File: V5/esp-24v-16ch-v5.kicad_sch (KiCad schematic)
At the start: 4 parts, among them J1 DB141V-2.54-8P, J2 DB141V-2.54-8P, J3 DB141V-2.54-8P, J4 DB141V-2.54-8P

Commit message: Created V5
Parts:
- added FID1, FID2, FID3: Fiducial, Fiducial:Fiducial_1mm_Mask2mm, symbol Mechanical:Fiducial
- renumbered J1 to J5, J2 to J6, J3 to J7, J4 to J8
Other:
- sheet I2C Devices: file esp-24v-16ch-v4-i2c.kicad_sch -> esp-24v-16ch-v5-i2c.kicad_sch
- sheet I2C Devices ports: added I2CSCL, I2CSDA, MCPININTA, MCPININTB; removed I2C_SCL, I2C_SDA, MCP1-INTA, MCP1-INTB
- sheet Input 1: file esp-24v-16ch-v4-inputs.kicad_sch -> esp-24v-16ch-v5-inputs1-8.kicad_sch
- sheet Input 1 ports: added MUXIN; removed MUX_IN
- sheet Input 10: file esp-24v-16ch-v4-inputs.kicad_sch -> esp-24v-16ch-v5-inputs9-16.kicad_sch
- sheet Input 10 ports: added MUXIN; removed MUX_IN
- sheet Input 11: file esp-24v-16ch-v4-inputs.kicad_sch -> esp-24v-16ch-v5-inputs9-16.kicad_sch
- sheet Input 11 ports: added MUXIN; removed MUX_IN
- sheet Input 12: file esp-24v-16ch-v4-inputs.kicad_sch -> esp-24v-16ch-v5-inputs9-16.kicad_sch
- sheet Input 12 ports: added MUXIN; removed MUX_IN
- sheet Input 13: file esp-24v-16ch-v4-inputs.kicad_sch -> esp-24v-16ch-v5-inputs9-16.kicad_sch
- sheet Input 13 ports: added MUXIN; removed MUX_IN
- sheet Input 14: file esp-24v-16ch-v4-inputs.kicad_sch -> esp-24v-16ch-v5-inputs9-16.kicad_sch
- sheet Input 14 ports: added MUXIN; removed MUX_IN
- sheet Input 15: file esp-24v-16ch-v4-inputs.kicad_sch -> esp-24v-16ch-v5-inputs9-16.kicad_sch
- sheet Input 15 ports: added MUXIN; removed MUX_IN
- sheet Input 16: file esp-24v-16ch-v4-inputs.kicad_sch -> esp-24v-16ch-v5-inputs9-16.kicad_sch
- sheet Input 16 ports: added MUXIN; removed MUX_IN
- sheet Input 2: file esp-24v-16ch-v4-inputs.kicad_sch -> esp-24v-16ch-v5-inputs1-8.kicad_sch
- sheet Input 2 ports: added MUXIN; removed MUX_IN
- sheet Input 3: file esp-24v-16ch-v4-inputs.kicad_sch -> esp-24v-16ch-v5-inputs1-8.kicad_sch
- sheet Input 3 ports: added MUXIN; removed MUX_IN
- sheet Input 4: file esp-24v-16ch-v4-inputs.kicad_sch -> esp-24v-16ch-v5-inputs1-8.kicad_sch
- sheet Input 4 ports: added MUXIN; removed MUX_IN
- sheet Input 5: file esp-24v-16ch-v4-inputs.kicad_sch -> esp-24v-16ch-v5-inputs1-8.kicad_sch
- sheet Input 5 ports: added MUXIN; removed MUX_IN
- sheet Input 6: file esp-24v-16ch-v4-inputs.kicad_sch -> esp-24v-16ch-v5-inputs1-8.kicad_sch
- sheet Input 6 ports: added MUXIN; removed MUX_IN
- sheet Input 7: file esp-24v-16ch-v4-inputs.kicad_sch -> esp-24v-16ch-v5-inputs1-8.kicad_sch
- sheet Input 7 ports: added MUXIN; removed MUX_IN
- sheet Input 8: file esp-24v-16ch-v4-inputs.kicad_sch -> esp-24v-16ch-v5-inputs1-8.kicad_sch
- sheet Input 8 ports: added MUXIN; removed MUX_IN
- sheet Input 9: file esp-24v-16ch-v4-inputs.kicad_sch -> esp-24v-16ch-v5-inputs9-16.kicad_sch
- sheet Input 9 ports: added MUXIN; removed MUX_IN
- sheet LAN: file esp-24v-16ch-v4-lan.kicad_sch -> esp-24v-16ch-v5-lan.kicad_sch
- sheet LAN ports: added EMACCLK, EMACMDC, EMACMDIO, EMACRX, EMACRXD0, EMACRXD1, EMACTXD0, EMACTXD1, EMACTXEN; removed EMAC_CLK, EMAC_MDC, EMAC_MDIO, EMAC_RX, EMAC_RXD0, EMAC_RXD1, EMAC_TXD0, EMAC_TXD1, EMAC_TXEN
- sheet MCU: file esp-24v-16ch-v4-mcu.kicad_sch -> esp-24v-16ch-v5-mcu.kicad_sch
- sheet MCU ports: added EMACCLK, EMACMDC, EMACMDIO, EMACRX, EMACRXD0, EMACRXD1, EMACTXD0, EMACTXD1, EMACTXEN, I2CSCL, I2CSDA, MCPININTA, MCPININTB, PHYPWR, USBD+, USBD-; removed EMAC_CLK, EMAC_MDC, EMAC_MDIO, EMAC_RX, EMAC_RXD0, EMAC_RXD1, EMAC_TXD0, EMAC_TXD1, EMAC_TXEN, I2C_SCL, I2C_SDA, MCP1-INTA, MCP1-INTB, PHY_PWR, USB_D+, USB_D-
- sheet Output 1: file esp-24v-16ch-outputs.kicad_sch -> esp-24v-16ch-v5-outputs1-8.kicad_sch
- sheet Output 1 ports: added MUXOUT; removed MUX_OUT
- sheet Output 10: file esp-24v-16ch-outputs.kicad_sch -> esp-24v-16ch-v5-outputs9-16.kicad_sch
- sheet Output 10 ports: added MUXOUT; removed MUX_OUT
- sheet Output 11: file esp-24v-16ch-outputs.kicad_sch -> esp-24v-16ch-v5-outputs9-16.kicad_sch
- sheet Output 11 ports: added MUXOUT; removed MUX_OUT
- sheet Output 12: file esp-24v-16ch-outputs.kicad_sch -> esp-24v-16ch-v5-outputs9-16.kicad_sch
- sheet Output 12 ports: added MUXOUT; removed MUX_OUT
- sheet Output 13: file esp-24v-16ch-outputs.kicad_sch -> esp-24v-16ch-v5-outputs9-16.kicad_sch
- sheet Output 13 ports: added MUXOUT; removed MUX_OUT
- sheet Output 14: file esp-24v-16ch-outputs.kicad_sch -> esp-24v-16ch-v5-outputs9-16.kicad_sch
- sheet Output 14 ports: added MUXOUT; removed MUX_OUT
- sheet Output 15: file esp-24v-16ch-outputs.kicad_sch -> esp-24v-16ch-v5-outputs9-16.kicad_sch
- sheet Output 15 ports: added MUXOUT; removed MUX_OUT
- sheet Output 16: file esp-24v-16ch-outputs.kicad_sch -> esp-24v-16ch-v5-outputs9-16.kicad_sch
- sheet Output 16 ports: added MUXOUT; removed MUX_OUT
- sheet Output 2: file esp-24v-16ch-outputs.kicad_sch -> esp-24v-16ch-v5-outputs1-8.kicad_sch
- sheet Output 2 ports: added MUXOUT; removed MUX_OUT
- sheet Output 3: file esp-24v-16ch-outputs.kicad_sch -> esp-24v-16ch-v5-outputs1-8.kicad_sch
- sheet Output 3 ports: added MUXOUT; removed MUX_OUT
- sheet Output 4: file esp-24v-16ch-outputs.kicad_sch -> esp-24v-16ch-v5-outputs1-8.kicad_sch
- sheet Output 4 ports: added MUXOUT; removed MUX_OUT
- sheet Output 5: file esp-24v-16ch-outputs.kicad_sch -> esp-24v-16ch-v5-outputs1-8.kicad_sch
- sheet Output 5 ports: added MUXOUT; removed MUX_OUT
- sheet Output 6: file esp-24v-16ch-outputs.kicad_sch -> esp-24v-16ch-v5-outputs1-8.kicad_sch
- sheet Output 6 ports: added MUXOUT; removed MUX_OUT
- sheet Output 7: file esp-24v-16ch-outputs.kicad_sch -> esp-24v-16ch-v5-outputs1-8.kicad_sch
- sheet Output 7 ports: added MUXOUT; removed MUX_OUT
- sheet Output 8: file esp-24v-16ch-outputs.kicad_sch -> esp-24v-16ch-v5-outputs1-8.kicad_sch
- sheet Output 8 ports: added MUXOUT; removed MUX_OUT
- sheet Output 9: file esp-24v-16ch-outputs.kicad_sch -> esp-24v-16ch-v5-outputs9-16.kicad_sch
- sheet Output 9 ports: added MUXOUT; removed MUX_OUT
- sheet Power: file esp-24v-16ch-v4-power.kicad_sch -> esp-24v-16ch-v5-power.kicad_sch
- sheet Power ports: added PHYPWR, USBD+, USBD-; removed PHY_PWR, USB_D+, USB_D-
- title: ESP 24V 16xIn/16xOut/4xNTC Module -> ESP 24V 16xIn/16xOut/1-Wire Module

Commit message: Updates and corrections to SCH and PCB
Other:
- sheet I2C Devices ports: added 1WIREGPIO; removed none
- sheet MCU ports: added 1WIREGPIO; removed none
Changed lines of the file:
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@@
 	(wire
 		(pts
-			(xy 219.71 59.69) (xy 219.71 71.12)
+			(xy 215.9 59.69) (xy 215.9 71.12)
 		)
 		(stroke
@@
 	(wire
 		(pts
-			(xy 214.63 59.69) (xy 214.63 71.12)
+			(xy 210.82 59.69) (xy 210.82 71.12)
 		)
 		(stroke
@@
 	(wire
 		(pts
-			(xy 212.09 59.69) (xy 212.09 71.12)
+			(xy 208.28 59.69) (xy 208.28 71.12)
 		)
 		(stroke
@@
 	(wire
 		(pts
+			(xy 222.25 59.69) (xy 222.25 71.12)
+		)
+		(stroke
+			(width 0)
+			(type default)
+		)
+	)
+	(wire
+		(pts
 			(xy 39.37 193.04) (xy 43.18 193.04)
 		)
@@
 	(wire
 		(pts
-			(xy 222.25 59.69) (xy 222.25 71.12)
+			(xy 218.44 59.69) (xy 218.44 71.12)
 		)
 		(stroke
@@
 		)
 		(pin "I2CSDA" bidirectional
-			(at 219.71 71.12 90)
+			(at 215.9 71.12 90)
 			(effects
 				(font
@@
 		)
 		(pin "I2CSCL" input
-			(at 222.25 71.12 90)
+			(at 218.44 71.12 90)
 			(effects
 				(font
@@
 		)
 		(pin "MCPININTB" output
-			(at 214.63 71.12 90)
+			(at 210.82 71.12 90)
 			(effects
 				(font
@@
 		)
 		(pin "MCPININTA" output
-			(at 212.09 71.12 90)
+			(at 208.28 71.12 90)
+			(effects
+				(font
+					(size 1.27 1.27)
+				)
+				(justify right)
+			)
+		)
+		(pin "1WIREGPIO" bidirectional
+			(at 222.25 71.12 90)
 			(effects
 				(font
@@
 		)
 		(pin "I2CSDA" bidirectional
-			(at 219.71 59.69 270)
+			(at 215.9 59.69 270)
 			(effects
 				(font
@@
 		)
 		(pin "I2CSCL" output
-			(at 222.25 59.69 270)
+			(at 218.44 59.69 270)
 			(effects
 				(font
@@
 		)
 		(pin "MCPININTA" input
-			(at 212.09 59.69 270)
+			(at 208.28 59.69 270)
 			(effects
 				(font
@@
 		)
 		(pin "MCPININTB" input
-			(at 214.63 59.69 270)
+			(at 210.82 59.69 270)
 			(effects
 				(font
@@
 			(effects
 				(font
+					(size 1.27 1.27)
+				)
+				(justify left)
+			)
+		)
+		(pin "1WIREGPIO" bidirectional
+			(at 222.25 59.69 270)
+			(effects
+				(font

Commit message: V5.2.0
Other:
- sheet MCU ports: added ESPEN; removed none
- sheet Power ports: added ESPEN; removed none
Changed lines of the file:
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@@
 	(wire
 		(pts
+			(xy 146.05 49.53) (xy 165.1 49.53)
+		)
+		(stroke
+			(width 0)
+			(type default)
+		)
+	)
+	(wire
+		(pts
 			(xy 276.86 166.37) (xy 265.43 166.37)
 		)
@@
 			)
 		)
-		(pin "USBD+" input
+		(pin "USBD+" bidirectional
 			(at 146.05 41.91 0)
 			(effects
@@
 			)
 		)
-		(pin "USBD-" input
+		(pin "USBD-" bidirectional
 			(at 146.05 44.45 0)
 			(effects
@@
 			)
 		)
+		(pin "ESPEN" output
+			(at 146.05 49.53 0)
+			(effects
+				(font
+					(size 1.27 1.27)
+				)
+				(justify right)
+			)
+		)
 		(instances
 			(project "esp-24v-16ch-v5"
@@
 			)
 		)
-		(pin "USBD+" input
+		(pin "USBD+" bidirectional
 			(at 165.1 41.91 180)
 			(effects
@@
 			)
 		)
-		(pin "USBD-" input
+		(pin "USBD-" bidirectional
 			(at 165.1 44.45 180)
 			(effects
@@
 			(effects
 				(font
+					(size 1.27 1.27)
+				)
+				(justify left)
+			)
+		)
+		(pin "ESPEN" input
+			(at 165.1 49.53 180)
+			(effects
+				(font

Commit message: Back to V5.1.0
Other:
- sheet MCU ports: added none; removed ESPEN
- sheet Power ports: added none; removed ESPEN
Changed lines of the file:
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@@
 	(wire
 		(pts
-			(xy 146.05 49.53) (xy 165.1 49.53)
-		)
-		(stroke
-			(width 0)
-			(type default)
-		)
-	)
-	(wire
-		(pts
 			(xy 276.86 166.37) (xy 265.43 166.37)
 		)
@@
 			)
 		)
-		(pin "ESPEN" output
-			(at 146.05 49.53 0)
-			(effects
-				(font
-					(size 1.27 1.27)
-				)
-				(justify right)
-			)
-		)
 		(instances
 			(project "esp-24v-16ch-v5"
@@
 			(effects
 				(font
-					(size 1.27 1.27)
-				)
-				(justify left)
-			)
-		)
-		(pin "ESPEN" input
-			(at 165.1 49.53 180)
-			(effects
-				(font

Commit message: Many changes!
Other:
- note added: "RESISTORS: 62,5mW WHERE NOT SPECIFIED"
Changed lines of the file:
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@@
 		(rev "V5.1")
+	)
+	(text "RESISTORS: 62,5mW WHERE NOT SPECIFIED"
+		(exclude_from_sim no)
+		(at 303.53 259.08 0)
+		(effects
+			(font
+				(size 1.905 1.905)
+			)
+			(justify left)
+		)
 	)
 	(wire

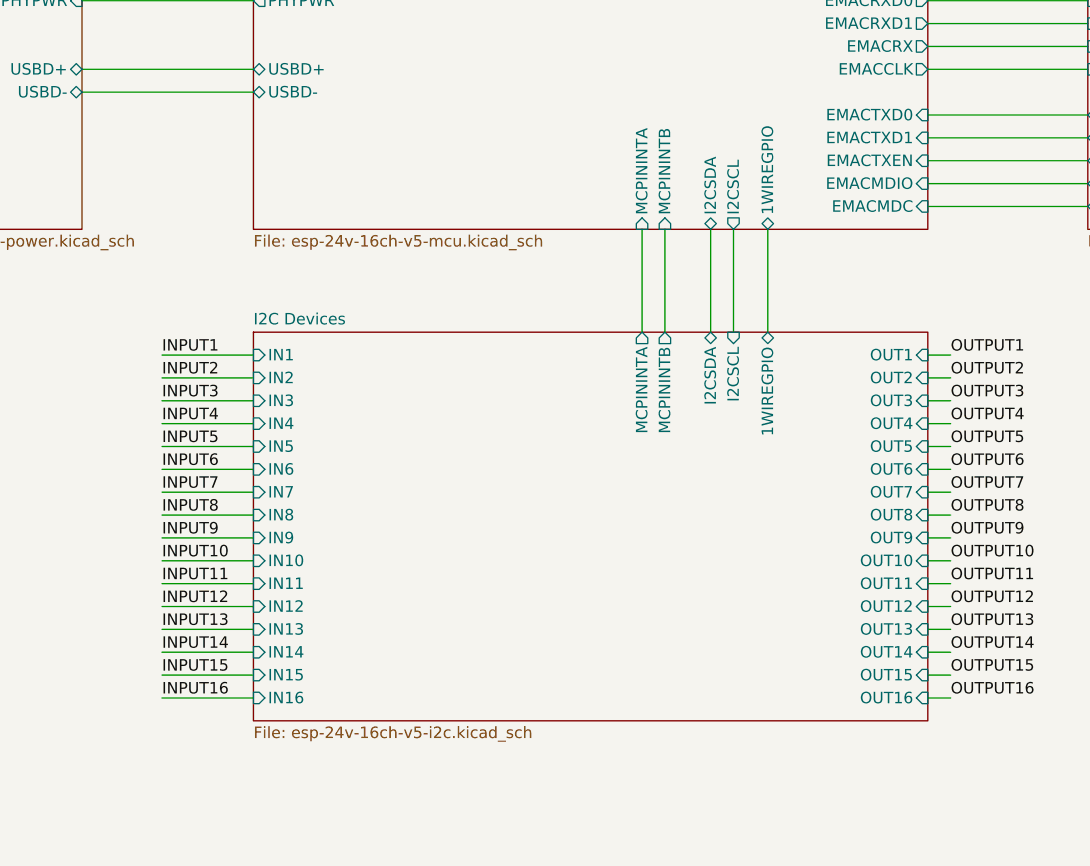
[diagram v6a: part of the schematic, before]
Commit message: MCP23017 GPA7 and GPB7 disabled.
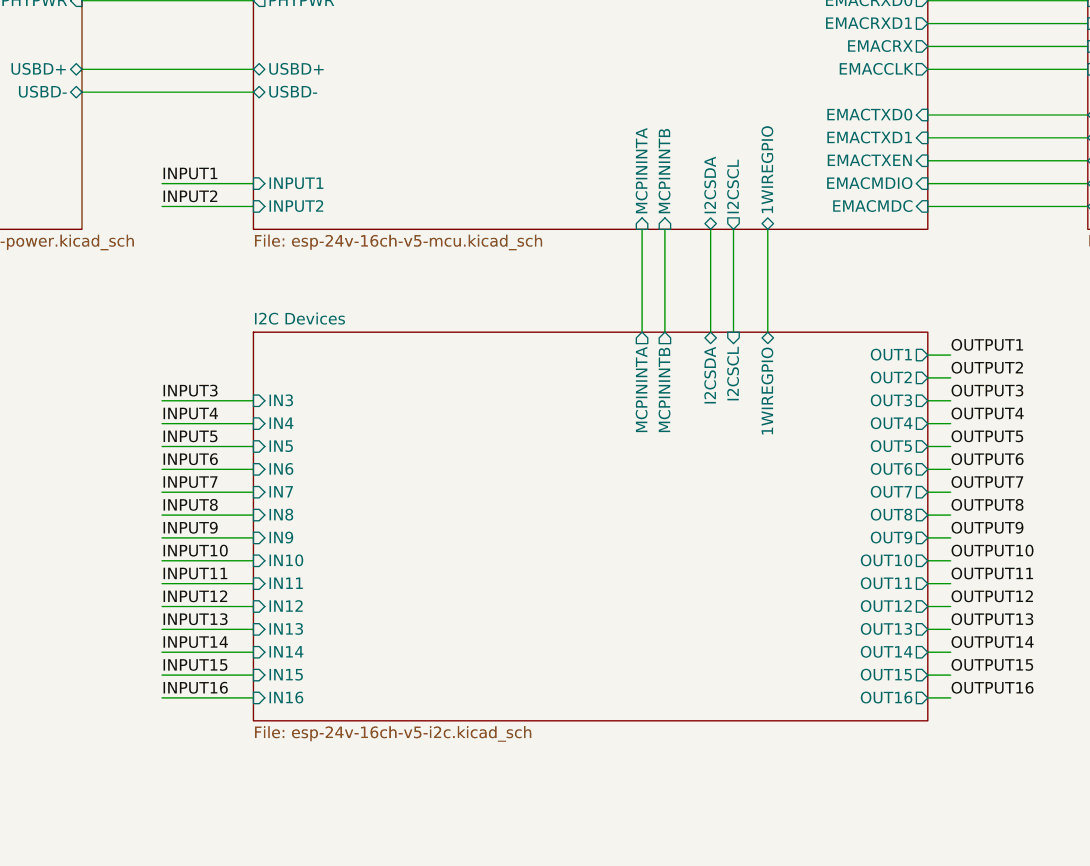
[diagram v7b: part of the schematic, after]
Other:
- sheet I2C Devices ports: added none; removed IN1, IN2
- sheet MCU ports: added INPUT1, INPUT2; removed none
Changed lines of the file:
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@@
 	(wire
 		(pts
-			(xy 154.94 73.66) (xy 165.1 73.66)
+			(xy 154.94 54.61) (xy 165.1 54.61)
 		)
 		(stroke
@@
 	(wire
 		(pts
-			(xy 154.94 76.2) (xy 165.1 76.2)
+			(xy 154.94 57.15) (xy 165.1 57.15)
 		)
 		(stroke
@@
 	)
 	(label "INPUT1"
-		(at 154.94 73.66 0)
+		(at 154.94 54.61 0)
 		(effects
 			(font
@@
 	)
 	(label "INPUT2"
-		(at 154.94 76.2 0)
+		(at 154.94 57.15 0)
 		(effects
 			(font
@@
 			)
 		)
-		(pin "IN2" input
-			(at 165.1 76.2 180)
-			(effects
-				(font
-					(size 1.27 1.27)
-				)
-				(justify left)
-			)
-		)
 		(pin "IN3" input
 			(at 165.1 78.74 180)
@@
 			)
 		)
-		(pin "IN1" input
-			(at 165.1 73.66 180)
+		(pin "IN15" input
+			(at 165.1 109.22 180)
 			(effects
 				(font
@@
 			)
 		)
-		(pin "OUT14" input
-			(at 240.03 106.68 0)
+		(pin "IN16" input
+			(at 165.1 111.76 180)
 			(effects
 				(font
 					(size 1.27 1.27)
 				)
-				(justify right)
+				(justify left)
 			)
 		)
-		(pin "OUT16" input
-			(at 240.03 111.76 0)
+		(pin "IN9" input
+			(at 165.1 93.98 180)
 			(effects
 				(font
 					(size 1.27 1.27)
 				)
-				(justify right)
+				(justify left)
 			)
 		)
-		(pin "OUT15" input
-			(at 240.03 109.22 0)
+		(pin "IN11" input
+			(at 165.1 99.06 180)
 			(effects
 				(font
 					(size 1.27 1.27)
 				)
-				(justify right)
+				(justify left)
 			)
 		)
-		(pin "OUT13" input
-			(at 240.03 104.14 0)
+		(pin "IN10" input
+			(at 165.1 96.52 180)
 			(effects
 				(font
 					(size 1.27 1.27)
 				)
-				(justify right)
+				(justify left)
 			)
 		)
-		(pin "OUT9" input
-			(at 240.03 93.98 0)
+		(pin "IN12" input
+			(at 165.1 101.6 180)
 			(effects
 				(font
 					(size 1.27 1.27)
 				)
-				(justify right)
+				(justify left)
 			)
 		)
-		(pin "OUT10" input
-			(at 240.03 96.52 0)
+		(pin "IN14" input
+			(at 165.1 106.68 180)
 			(effects
 				(font
 					(size 1.27 1.27)
 				)
-				(justify right)
+				(justify left)
 			)
 		)
-		(pin "OUT11" input
-			(at 240.03 99.06 0)
+		(pin "IN13" input
+			(at 165.1 104.14 180)
 			(effects
 				(font
 					(size 1.27 1.27)
 				)
-				(justify right)
+				(justify left)
 			)
 		)
-		(pin "OUT12" input
-			(at 240.03 101.6 0)
+		(pin "I2CSDA" bidirectional
+			(at 215.9 71.12 90)
 			(effects
 				(font
@@
 			)
 		)
-		(pin "IN15" input
-			(at 165.1 109.22 180)
-			(effects
-				(font
-					(size 1.27 1.27)
-				)
-				(justify left)
-			)
-		)
-		(pin "IN16" input
-			(at 165.1 111.76 180)
+		(pin "I2CSCL" input
+			(at 218.44 71.12 90)
 			(effects
 				(font
 					(size 1.27 1.27)
 				)
-				(justify left)
+				(justify right)
 			)
 		)
-		(pin "IN9" input
-			(at 165.1 93.98 180)
+		(pin "MCPININTB" output
+			(at 210.82 71.12 90)
 			(effects
 				(font
 					(size 1.27 1.27)
 				)
-				(justify left)
+				(justify right)
 			)
 		)
-		(pin "IN11" input
-			(at 165.1 99.06 180)
+		(pin "MCPININTA" output
+			(at 208.28 71.12 90)
 			(effects
 				(font
 					(size 1.27 1.27)
 				)
-				(justify left)
+				(justify right)
 			)
 		)
-		(pin "IN10" input
-			(at 165.1 96.52 180)
+		(pin "1WIREGPIO" bidirectional
+			(at 222.25 71.12 90)
 			(effects
 				(font
 					(size 1.27 1.27)
 				)
-				(justify left)
+				(justify right)
 			)
 		)
-		(pin "IN12" input
-			(at 165.1 101.6 180)
+		(pin "OUT1" output
+			(at 240.03 73.66 0)
 			(effects
 				(font
 					(size 1.27 1.27)
 				)
-				(justify left)
+				(justify right)
 			)
 		)
-		(pin "IN14" input
-			(at 165.1 106.68 180)
+		(pin "OUT2" output
+			(at 240.03 76.2 0)
 			(effects
 				(font
 					(size 1.27 1.27)
 				)
-				(justify left)
+				(justify right)
 			)
 		)
-		(pin "IN13" input
-			(at 165.1 104.14 180)
+		(pin "OUT3" output
+			(at 240.03 78.74 0)
 			(effects
 				(font
 					(size 1.27 1.27)
 				)
-				(justify left)
+				(justify right)
 			)
 		)
-		(pin "OUT4" input
+		(pin "OUT4" output
 			(at 240.03 81.28 0)
 			(effects
@@
 			)
 		)
-		(pin "OUT3" input
-			(at 240.03 78.74 0)
+		(pin "OUT5" output
+			(at 240.03 83.82 0)
 			(effects
 				(font
@@
 			)
 		)
-		(pin "OUT5" input
-			(at 240.03 83.82 0)
+		(pin "OUT6" output
+			(at 240.03 86.36 0)
 			(effects
 				(font
@@
 			)
 		)
-		(pin "OUT7" input
+		(pin "OUT7" output
 			(at 240.03 88.9 0)
 			(effects
@@
 			)
 		)
-		(pin "OUT6" input
-			(at 240.03 86.36 0)
+		(pin "OUT8" output
+			(at 240.03 91.44 0)
 			(effects
 				(font
@@
 			)
 		)
-		(pin "OUT8" input
-			(at 240.03 91.44 0)
+		(pin "OUT9" output
+			(at 240.03 93.98 0)
 			(effects
 				(font
@@
 			)
 		)
-		(pin "OUT2" input
-			(at 240.03 76.2 0)
+		(pin "OUT10" output
+			(at 240.03 96.52 0)
 			(effects
 				(font
@@
 			)
 		)
-		(pin "OUT1" input
-			(at 240.03 73.66 0)
+		(pin "OUT11" output
+			(at 240.03 99.06 0)
 			(effects
 				(font
@@
 			)
 		)
-		(pin "I2CSDA" bidirectional
-			(at 215.9 71.12 90)
+		(pin "OUT12" output
+			(at 240.03 101.6 0)
 			(effects
 				(font
@@
 			)
 		)
-		(pin "I2CSCL" input
-			(at 218.44 71.12 90)
+		(pin "OUT13" output
+			(at 240.03 104.14 0)
 			(effects
 				(font
@@
 			)
 		)
-		(pin "MCPININTB" output
-			(at 210.82 71.12 90)
+		(pin "OUT14" output
+			(at 240.03 106.68 0)
 			(effects
 				(font
@@
 			)
 		)
-		(pin "MCPININTA" output
-			(at 208.28 71.12 90)
+		(pin "OUT15" output
+			(at 240.03 109.22 0)
 			(effects
 				(font
@@
 			)
 		)
-		(pin "1WIREGPIO" bidirectional
-			(at 222.25 71.12 90)
+		(pin "OUT16" output
+			(at 240.03 111.76 0)
 			(effects
 				(font
@@
 			(effects
 				(font
+					(size 1.27 1.27)
+				)
+				(justify left)
+			)
+		)
+		(pin "INPUT1" input
+			(at 165.1 54.61 180)
+			(effects
+				(font
+					(size 1.27 1.27)
+				)
+				(justify left)
+			)
+		)
+		(pin "INPUT2" input
+			(at 165.1 57.15 180)
+			(effects
+				(font
